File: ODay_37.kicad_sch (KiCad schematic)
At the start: 12 parts, among them SW1 Rotary Battery Select, U1 Renogy BC50D1S Solar Controll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, U2 Dual_10A_Battery_Charger

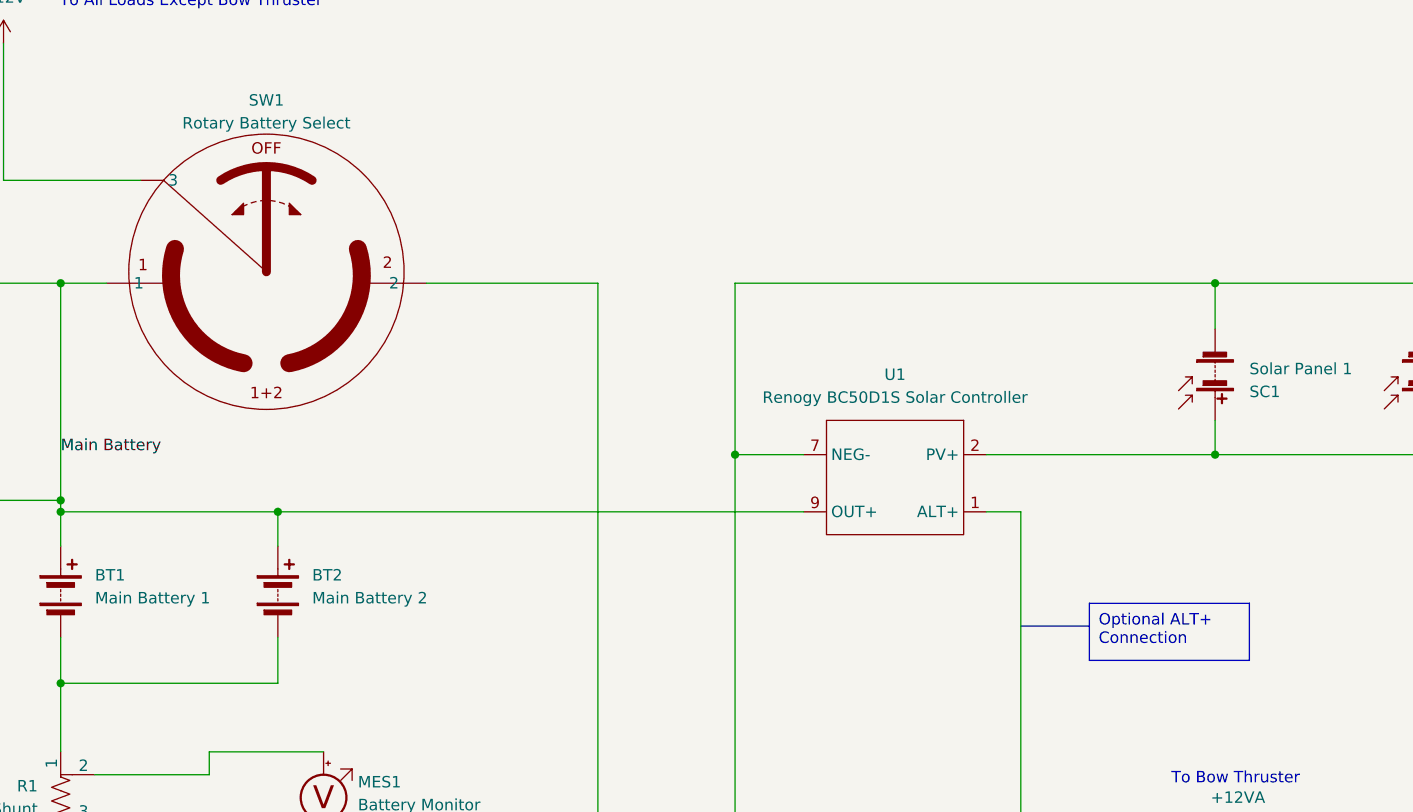
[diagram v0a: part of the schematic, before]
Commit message: Add descriptive info to title block
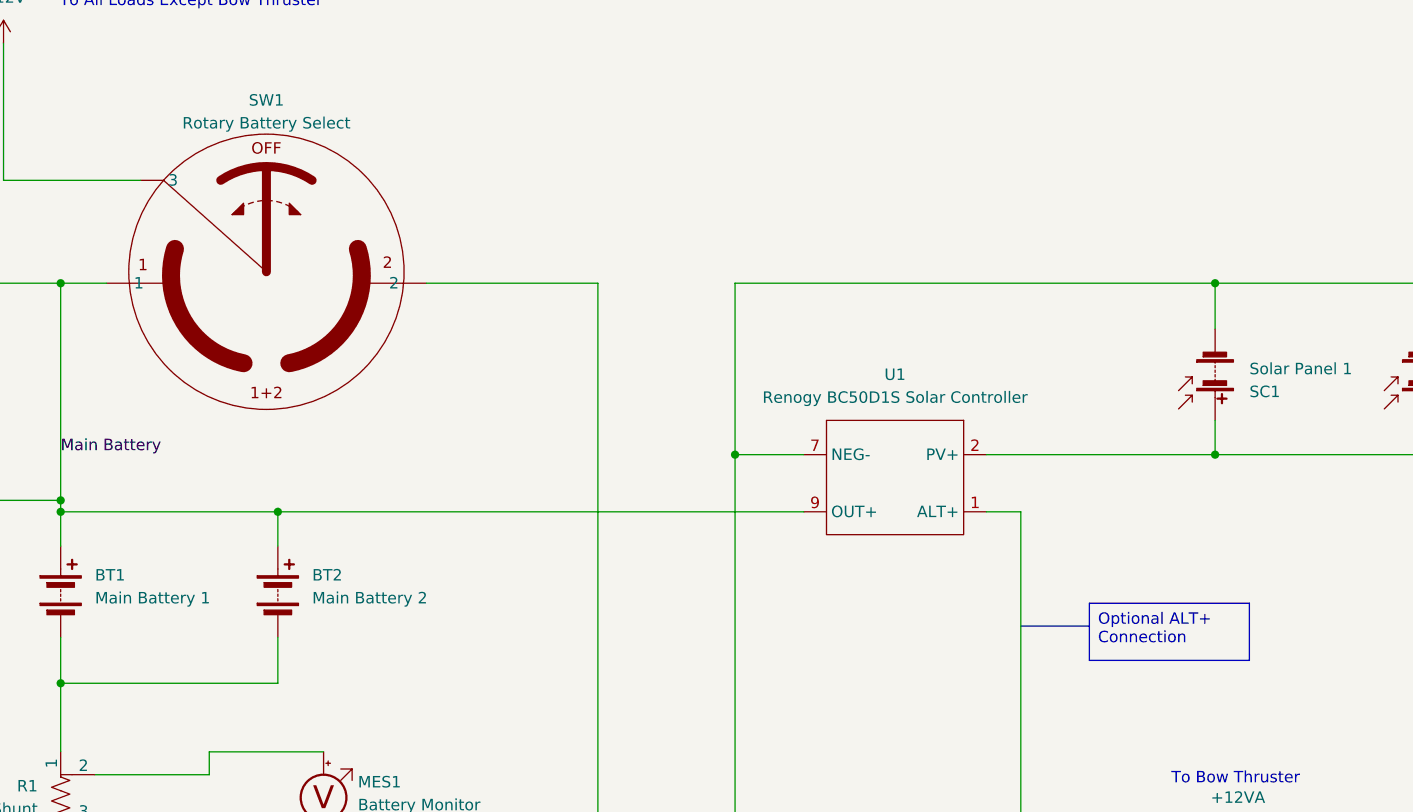
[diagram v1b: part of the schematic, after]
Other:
- title: (none) -> ODay 37 12VDC Battery/Generator/Solar Details
